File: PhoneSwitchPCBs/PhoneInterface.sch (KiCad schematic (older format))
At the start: 53 parts, among them J1 Interface, J2 6P2C, K1 EC2-5NU, K2 EC2-5NU, K3 EC2-5NU, K4 EC2-5NU, K5 EC2-5NU, Q1 PHPT61003PYX, Q2 PHPT61003NYX, Q3 XP231N02013R-G, Q4 XP231N02013R-G, Q5 XP231N02013R-G, Q6 XP231N02013R-G, U1 TCMD1000, U2 NL17SZ14DBVT1G

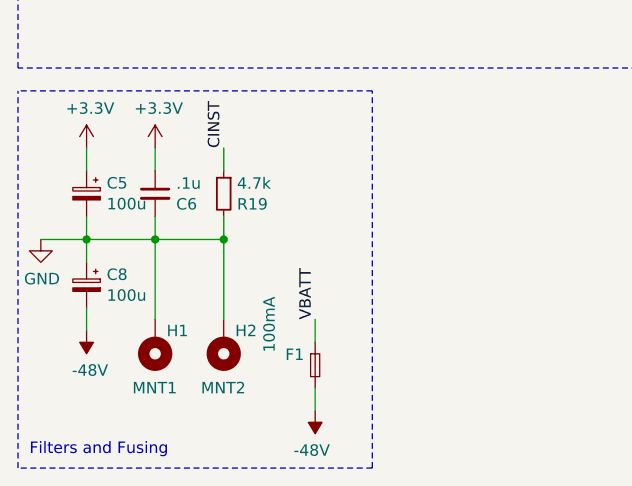
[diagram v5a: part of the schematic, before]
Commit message: More progress, added two extra mounting holes
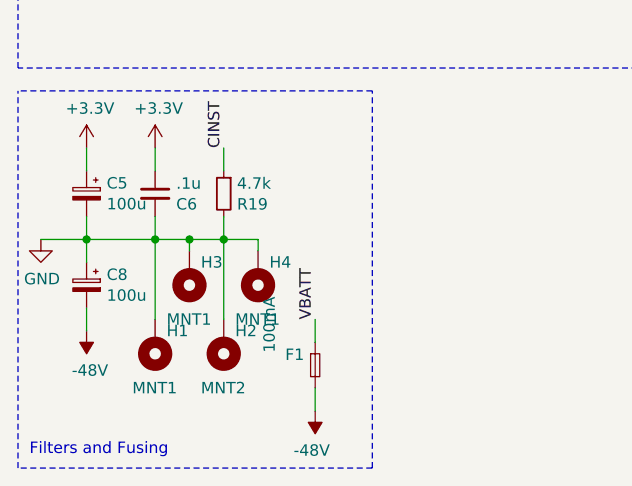
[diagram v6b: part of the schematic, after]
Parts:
- added H3, H4: MNT1, MountingHole:MountingHole_2.7mm_M2.5_Pad, symbol Mechanical:MountingHole_Pad
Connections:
- net GND: now also H3.1, H4.1
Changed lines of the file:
@@
 	1350 5700 1050 5700
 Wire Wire Line
-	1650 5700 1350 5700
+	1650 5700 1500 5700
 Connection ~ 1350 5700
 Text Label 1300 1800 2    50   ~ 0
@@
 Wire Wire Line
 	1350 5700 1350 6050
+$Comp
+L Mechanical:MountingHole_Pad H3
+U 1 1 612247FE
+P 1500 5850
+F 0 "H3" H 1450 5800 50  0000 R CNN
+F 1 "MNT1" H 1600 6050 50  0000 R CNN
+F 2 "MountingHole:MountingHole_2.7mm_M2.5_Pad" H 1500 5850 50  0001 C CNN
+F 3 "~" H 1500 5850 50  0001 C CNN
+	1    1500 5850
+	-1   0    0    1
+$EndComp
+$Comp
+L Mechanical:MountingHole_Pad H4
+U 1 1 61225DDE
+P 1800 5850
+F 0 "H4" H 1750 5800 50  0000 R CNN
+F 1 "MNT1" H 1900 6050 50  0000 R CNN
+F 2 "MountingHole:MountingHole_2.7mm_M2.5_Pad" H 1800 5850 50  0001 C CNN
+F 3 "~" H 1800 5850 50  0001 C CNN
+	1    1800 5850
+	-1   0    0    1
+$EndComp
+Wire Wire Line
+	1800 5750 1800 5700
+Wire Wire Line
+	1800 5700 1650 5700
+Wire Wire Line
+	1500 5750 1500 5700
+Connection ~ 1500 5700
+Wire Wire Line
+	1500 5700 1350 5700
 $EndSCHEMATC
